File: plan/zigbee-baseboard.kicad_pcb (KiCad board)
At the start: 4 copper layers, 15.3 x 20.6 mm, 55 parts, among them J1 Debug_SWD_Pogo_2x3_P2.00mm, J2 EFR32MG24_Core_Expansion_L12, SW1 EVPBB2A9B000, U1 EFR32MG24B020F1536IM48-B, Y1 XTL501250-S315-038

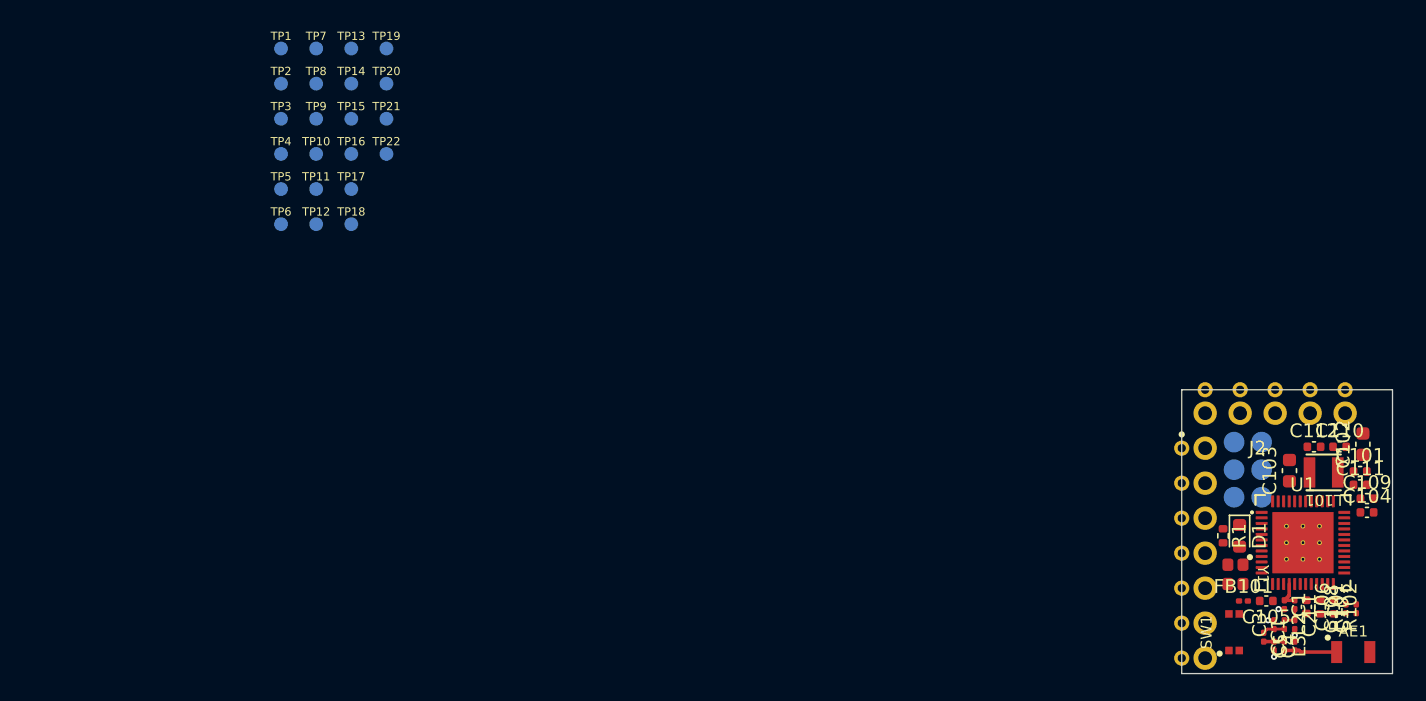
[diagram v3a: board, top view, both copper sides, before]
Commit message: Basic placement of GPIO pads on bottom side
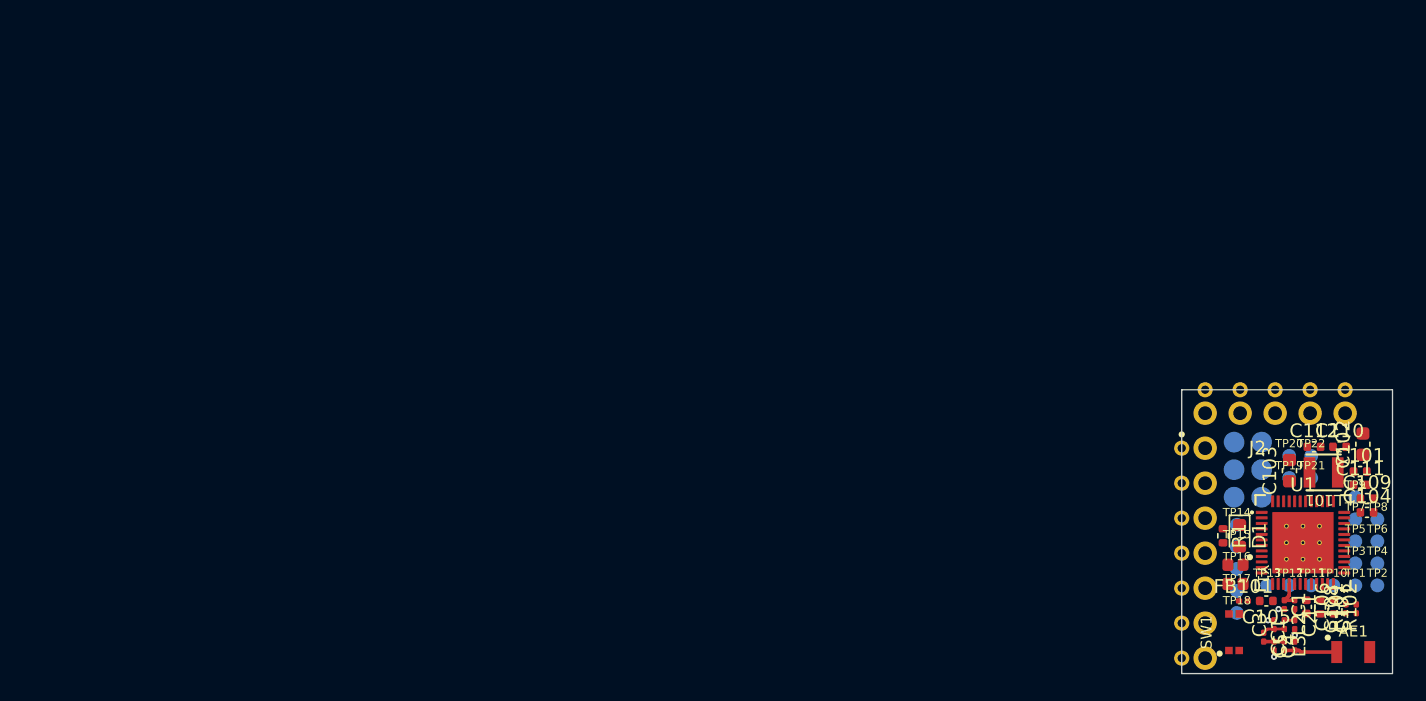
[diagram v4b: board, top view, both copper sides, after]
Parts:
- moved TP2 87.5 mm to (148.4, 96.6)
- moved TP1 87.2 mm to (146.8, 96.6)
- moved TP4 84.9 mm to (148.4, 95.0)
- moved TP3 84.4 mm to (146.8, 95.0)
- moved TP8 83.3 mm to (148.4, 91.8)
- moved TP6 82.8 mm to (148.4, 93.4)
- moved TP7 82.8 mm to (146.8, 91.8)
- moved TP5 82.1 mm to (146.8, 93.4)
- moved TP9 80.3 mm to (146.8, 90.2)
- moved TP10 80.2 mm to (145.2, 96.6)
- moved TP11 77.7 mm to (143.6, 96.6)
- moved TP13 77.1 mm to (140.4, 96.6)
- moved TP12 75.3 mm to (142.0, 96.6)
- moved TP19 72.6 mm to (142.0, 88.8)
- moved TP21 72.0 mm to (143.6, 88.8)
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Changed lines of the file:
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@@
 	(footprint "Smarthome:GPIO_SolderPad_D1.0mm_Bottom"
 		(layer "F.Cu")
-		(at 76.475 65.28)
+		(at 143.6 87.2)
 		(property "Reference" "TP22"
 			(at 0 -0.9 0)
@@
 	(footprint "Smarthome:GPIO_SolderPad_D1.0mm_Bottom"
 		(layer "F.Cu")
-		(at 71.375 57.63)
+		(at 146.8 91.8)
 		(property "Reference" "TP7"
 			(at 0 -0.9 0)
@@
 	(footprint "Smarthome:GPIO_SolderPad_D1.0mm_Bottom"
 		(layer "F.Cu")
-		(at 71.375 65.28)
+		(at 145.2 96.6)
 		(property "Reference" "TP10"
 			(at 0 -0.9 0)
@@
 	(footprint "Smarthome:GPIO_SolderPad_D1.0mm_Bottom"
 		(layer "F.Cu")
-		(at 68.825 62.73)
+		(at 146.8 95)
 		(property "Reference" "TP3"
 			(at 0 -0.9 0)
@@
 	(footprint "Smarthome:GPIO_SolderPad_D1.0mm_Bottom"
 		(layer "F.Cu")
-		(at 68.825 70.38)
+		(at 148.4 93.4)
 		(property "Reference" "TP6"
 			(at 0 -0.9 0)
@@
 	(footprint "Smarthome:GPIO_SolderPad_D1.0mm_Bottom"
 		(layer "F.Cu")
-		(at 71.375 62.73)
+		(at 146.8 90.2)
 		(property "Reference" "TP9"
 			(at 0 -0.9 0)
@@
 	(footprint "Smarthome:GPIO_SolderPad_D1.0mm_Bottom"
 		(layer "F.Cu")
-		(at 76.475 57.63)
+		(at 142 88.8)
 		(property "Reference" "TP19"
 			(at 0 -0.9 0)
@@
 	(footprint "Smarthome:GPIO_SolderPad_D1.0mm_Bottom"
 		(layer "F.Cu")
-		(at 73.925 60.18)
+		(at 138.2 92.2)
 		(property "Reference" "TP14"
 			(at 0 -0.9 0)
@@
 	(footprint "Smarthome:GPIO_SolderPad_D1.0mm_Bottom"
 		(layer "F.Cu")
-		(at 73.925 62.73)
+		(at 138.2 93.8)
 		(property "Reference" "TP15"
 			(at 0 -0.9 0)
@@
 	(footprint "Smarthome:GPIO_SolderPad_D1.0mm_Bottom"
 		(layer "F.Cu")
-		(at 73.925 67.83)
+		(at 138.2 97)
 		(property "Reference" "TP17"
 			(at 0 -0.9 0)
@@
 	(footprint "Smarthome:GPIO_SolderPad_D1.0mm_Bottom"
 		(layer "F.Cu")
-		(at 68.825 60.18)
+		(at 148.4 96.6)
 		(property "Reference" "TP2"
 			(at 0 -0.9 0)
@@
 	(footprint "Smarthome:GPIO_SolderPad_D1.0mm_Bottom"
 		(layer "F.Cu")
-		(at 68.825 65.28)
+		(at 148.4 95)
 		(property "Reference" "TP4"
 			(at 0 -0.9 0)
@@
 	(footprint "Smarthome:GPIO_SolderPad_D1.0mm_Bottom"
 		(layer "F.Cu")
-		(at 71.375 60.18)
+		(at 148.4 91.8)
 		(property "Reference" "TP8"
 			(at 0 -0.9 0)
@@
 	(footprint "Smarthome:GPIO_SolderPad_D1.0mm_Bottom"
 		(layer "F.Cu")
-		(at 73.925 70.38)
+		(at 138.2 98.6)
 		(property "Reference" "TP18"
 			(at 0 -0.9 0)
@@
 	(footprint "Smarthome:GPIO_SolderPad_D1.0mm_Bottom"
 		(layer "F.Cu")
-		(at 73.925 65.28)
+		(at 138.2 95.4)
 		(property "Reference" "TP16"
 			(at 0 -0.9 0)
@@
 	(footprint "Smarthome:GPIO_SolderPad_D1.0mm_Bottom"
 		(layer "F.Cu")
-		(at 76.475 62.73)
+		(at 143.6 88.8)
 		(property "Reference" "TP21"
 			(at 0 -0.9 0)
@@
 	(footprint "Smarthome:GPIO_SolderPad_D1.0mm_Bottom"
 		(layer "F.Cu")
-		(at 68.825 57.63)
+		(at 146.8 96.6)
 		(property "Reference" "TP1"
 			(at 0 -0.9 0)
@@
 	(footprint "Smarthome:GPIO_SolderPad_D1.0mm_Bottom"
 		(layer "F.Cu")
-		(at 71.375 67.83)
+		(at 143.6 96.6)
 		(property "Reference" "TP11"
 			(at 0 -0.9 0)
@@
 	(footprint "Smarthome:GPIO_SolderPad_D1.0mm_Bottom"
 		(layer "F.Cu")
-		(at 68.825 67.83)
+		(at 146.8 93.4)
 		(property "Reference" "TP5"
 			(at 0 -0.9 0)
@@
 	(footprint "Smarthome:GPIO_SolderPad_D1.0mm_Bottom"
 		(layer "F.Cu")
-		(at 73.925 57.63)
+		(at 140.4 96.6)
 		(property "Reference" "TP13"
 			(at 0 -0.9 0)
@@
 	(footprint "Smarthome:GPIO_SolderPad_D1.0mm_Bottom"
 		(layer "F.Cu")
-		(at 71.375 70.38)
+		(at 142 96.6)
 		(property "Reference" "TP12"
 			(at 0 -0.9 0)
@@
 	(footprint "Smarthome:GPIO_SolderPad_D1.0mm_Bottom"
 		(layer "F.Cu")
-		(at 76.475 60.18)
+		(at 142 87.2)
 		(property "Reference" "TP20"
 			(at 0 -0.9 0)
